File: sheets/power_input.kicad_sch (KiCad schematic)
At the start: 106 parts, among them J2 TYPE-C-31-M-12, Q20 FDMS86250, Q21 FDMC2523P, Q22 BSC057N08NS3 G, Q23 BSC057N08NS3 G, Q24 FCX493TA, Q25 FCX493TA, Q30 IRLR7843TRPBF, Q31 IRLR7843TRPBF, T1 750313355, U10 TPS23730RMTR, U19 LM5050MKX-1/NOPB, U2 CH224K, U20 TCMT1107, U21 LM5050MKX-1/NOPB, U22 TL431IDBVR, U23 FOD817DS

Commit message: sch: audit fixes — buck EN divider corners, 3V3-domain senses, spec §10 LEDs
F1 (critical): TPS565201 BUCK_EN divider (R40/R41) redesigned against the
datasheet's VENH/VENL/REN corners so the 3.3V buck actually starts once the
12V node is negotiated, without false-starting on pre-negotiation 5V VBUS.

F2 (medium): GP18/GP19 retargeted from the RP2040 sheet to the ethernet
sheet's existing 3.3V-domain PERST/CLKREQ shifter outputs; GP17 gets a new
BSS138 level-shift stage (Q40/R122) on m2, mirroring the Task 10 pattern.

F3 (minor): added the two spec §10 indicator LEDs (D29 12V/power, D30
PD-good) that were dropped during Task 4 and never restored.

check_nets.py all pass; ERC 0 errors / 800 warnings (was 788, full delta
accounted in docs/erc-waivers.md); netlist exports clean, no annotation
warnings.

Co-Authored-By: Claude Fable 5 <noreply@anthropic.com>
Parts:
- added D29: Green 0603, LED_0603, symbol Device:LED
- added D30: Blue 0603, LED_0603, symbol Device:LED
- added R120, R121: 1k, R_0603, symbol Device:R_Small
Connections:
- net CH224K_PG: now also D30.1 (K)
- net GND: now also D29.1 (K)
- new net LED_PWR: R120.1, R121.1
- new net N_D29_A: D29.2 (A), R120.2
- new net N_D30_A: D30.2 (A), R121.2
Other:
- note added: "Task 13 audit fix (F3, minor): D29/R120 -- spec S10 12V-node/power indicator, missing since Task 4 dropped the LED (drift, never amended). LED_PWR->R120(1k)->D29->GND. LED_PWR is only alive when +3V3 is up, which -- per the F1 fix pass (R40/R41 BUCK_EN divider corrected) -- only happens once the +12V node has been negotiated (buck now reliably starts ~8V+, never at 5V pre-negotiation). So D29 cor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"
- note added: "Task 13 audit fix (F3, minor): D30/R121 -- spec S10 PD-good indicator, missing since Task 4 dropped the LED. LED_PWR->R121(1k)->D30->CH224K_PG. CH224K_PG is open-drain, active-low (WCH CH224K datasheet: pulls to GND once PD negotiation succeeds; datasheet explicitly lists driving an indicator LED as a typical use). Checked R4 (10k pull-up, CH224K_PG to +3V3, from Task 4): it does NOT conflict wit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"
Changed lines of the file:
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@@
 	)
 	(symbol
+		(lib_id "Device:LED")
+		(at 115 20 0)
+		(unit 1)
+		(exclude_from_sim no)
+		(in_bom yes)
+		(on_board yes)
+		(dnp no)
+		(fields_autoplaced yes)
+		(property "Reference" "D30" (at 117 17 0) (effects (font (size 1.27 1.27))))
+		(property "Value" "Blue 0603" (at 117 23 0) (effects (font (size 1.27 1.27))))
+		(property "Footprint" "LED_0603" (at 115 20 0) (hide yes) (effects (font (size 1.27 1.27))))
+		(property "Datasheet" "" (at 115 20 0) (hide yes) (effects (font (size 1.27 1.27))))
+		(pin "1")
+		(pin "2")
+		(instances
+			(project "sierra-to-usb"
+				(path "/f141b3c0-0a69-4819-acb0-dc32f46a3541/f5a12b4b-c279-4b26-9f14-8d152bf2e4b9"
+					(reference "D30")
+					(unit 1)
+				)
+			)
+		)
+	)
+	(symbol
+		(lib_id "Device:R_Small")
+		(at 115 27 0)
+		(unit 1)
+		(exclude_from_sim no)
+		(in_bom yes)
+		(on_board yes)
+		(dnp no)
+		(fields_autoplaced yes)
+		(property "Reference" "R121" (at 117 24 0) (effects (font (size 1.27 1.27))))
+		(property "Value" "1k" (at 117 30 0) (effects (font (size 1.27 1.27))))
+		(property "Footprint" "R_0603" (at 115 27 0) (hide yes) (effects (font (size 1.27 1.27))))
+		(property "Datasheet" "" (at 115 27 0) (hide yes) (effects (font (size 1.27 1.27))))
+		(pin "1")
+		(pin "2")
+		(instances
+			(project "sierra-to-usb"
+				(path "/f141b3c0-0a69-4819-acb0-dc32f46a3541/f5a12b4b-c279-4b26-9f14-8d152bf2e4b9"
+					(reference "R121")
+					(unit 1)
+				)
+			)
+		)
+	)
+	(symbol
 		(lib_id "sierra-to-usb:MB10S")
 		(at 150 30 0)
@@
 	)
 	(symbol
+		(lib_id "Device:LED")
+		(at 565 143 0)
+		(unit 1)
+		(exclude_from_sim no)
+		(in_bom yes)
+		(on_board yes)
+		(dnp no)
+		(fields_autoplaced yes)
+		(property "Reference" "D29" (at 567 140 0) (effects (font (size 1.27 1.27))))
+		(property "Value" "Green 0603" (at 567 146 0) (effects (font (size 1.27 1.27))))
+		(property "Footprint" "LED_0603" (at 565 143 0) (hide yes) (effects (font (size 1.27 1.27))))
+		(property "Datasheet" "" (at 565 143 0) (hide yes) (effects (font (size 1.27 1.27))))
+		(pin "1")
+		(pin "2")
+		(instances
+			(project "sierra-to-usb"
+				(path "/f141b3c0-0a69-4819-acb0-dc32f46a3541/f5a12b4b-c279-4b26-9f14-8d152bf2e4b9"
+					(reference "D29")
+					(unit 1)
+				)
+			)
+		)
+	)
+	(symbol
+		(lib_id "Device:R_Small")
+		(at 565 150 0)
+		(unit 1)
+		(exclude_from_sim no)
+		(in_bom yes)
+		(on_board yes)
+		(dnp no)
+		(fields_autoplaced yes)
+		(property "Reference" "R120" (at 567 147 0) (effects (font (size 1.27 1.27))))
+		(property "Value" "1k" (at 567 153 0) (effects (font (size 1.27 1.27))))
+		(property "Footprint" "R_0603" (at 565 150 0) (hide yes) (effects (font (size 1.27 1.27))))
+		(property "Datasheet" "" (at 565 150 0) (hide yes) (effects (font (size 1.27 1.27))))
+		(pin "1")
+		(pin "2")
+		(instances
+			(project "sierra-to-usb"
+				(path "/f141b3c0-0a69-4819-acb0-dc32f46a3541/f5a12b4b-c279-4b26-9f14-8d152bf2e4b9"
+					(reference "R120")
+					(unit 1)
+				)
+			)
+		)
+	)
+	(symbol
+		(lib_id "power:GND")
+		(at 561.19 143 0)
+		(unit 1)
+		(exclude_from_sim no)
+		(in_bom yes)
+		(on_board yes)
+		(dnp no)
+		(fields_autoplaced yes)
+		(property "Reference" "#PWR9500001" (at 561.19 141.0 0) (hide yes) (effects (font (size 1.27 1.27))))
+		(property "Value" "GND" (at 561.19 139.0 0) (effects (font (size 1.27 1.27))))
+		(property "Footprint" "" (at 561.19 143 0) (hide yes) (effects (font (size 1.27 1.27))))
+		(property "Datasheet" "" (at 561.19 143 0) (hide yes) (effects (font (size 1.27 1.27))))
+		(pin "1")
+		(instances
+			(project "sierra-to-usb"
+				(path "/f141b3c0-0a69-4819-acb0-dc32f46a3541/f5a12b4b-c279-4b26-9f14-8d152bf2e4b9"
+					(reference "#PWR9500001")
+					(unit 1)
+				)
+			)
+		)
+	)
+	(symbol
 		(lib_id "sierra-to-usb:LM5050-1")
 		(at 580 30 0)
@@
 		(effects (font (size 1.27 1.27)) (justify left bottom))
 	)
+	(global_label "LED_PWR"
+		(shape input)
+		(at 565.0 147.46 0)
+		(effects (font (size 1.016 1.016)) (justify left bottom))
+		(property "Intersheetrefs" "${INTERSHEET_REFS}" (at 565.0 147.46 0) (effects (font (size 1.27 1.27))))
+	)
+	(label "N_D29_A"
+		(at 565.0 152.54 0)
+		(effects (font (size 1.016 1.016)) (justify left bottom))
+	)
+	(label "N_D29_A"
+		(at 568.81 143.0 0)
+		(effects (font (size 1.016 1.016)) (justify left bottom))
+	)
+	(global_label "LED_PWR"
+		(shape input)
+		(at 115.0 24.46 0)
+		(effects (font (size 1.016 1.016)) (justify left bottom))
+		(property "Intersheetrefs" "${INTERSHEET_REFS}" (at 115.0 24.46 0) (effects (font (size 1.27 1.27))))
+	)
+	(label "N_D30_A"
+		(at 115.0 29.54 0)
+		(effects (font (size 1.016 1.016)) (justify left bottom))
+	)
+	(label "N_D30_A"
+		(at 118.81 20.0 0)
+		(effects (font (size 1.016 1.016)) (justify left bottom))
+	)
+	(global_label "CH224K_PG"
+		(shape input)
+		(at 111.19 20.0 0)
+		(effects (font (size 1.016 1.016)) (justify left bottom))
+		(property "Intersheetrefs" "${INTERSHEET_REFS}" (at 111.19 20.0 0) (effects (font (size 1.27 1.27))))
+	)
+	(text "Task 13 audit fix (F3, minor): D29/R120 -- spec S10 12V-node/power indicator, missing since Task 4 dropped the LED (drift, never amended). LED_PWR->R120(1k)->D29->GND. LED_PWR is only alive when +3V3 is up, which -- per the F1 fix pass (R40/R41 BUCK_EN divider corrected) -- only happens once the +12V node has been negotiated (buck now reliably starts ~8V+, never at 5V pre-negotiation). So D29 correctly indicates negotiated-12V-present, not raw VBUS. It is killable via the LED_PWR switch/GPIO like the other LED_PWR-domain indicators (RGB, WWAN)."
+		(exclude_from_sim no)
+		(at 555 160 0)
+		(effects (font (size 1.27 1.27)) (justify left bottom))
+	)
+	(text "Task 13 audit fix (F3, minor): D30/R121 -- spec S10 PD-good indicator, missing since Task 4 dropped the LED. LED_PWR->R121(1k)->D30->CH224K_PG. CH224K_PG is open-drain, active-low (WCH CH224K datasheet: pulls to GND once PD negotiation succeeds; datasheet explicitly lists driving an indicator LED as a typical use). Checked R4 (10k pull-up, CH224K_PG to +3V3, from Task 4): it does NOT conflict with D30 -- it defines a clean idle-high (LED off) state when PG is unasserted and adds only ~0.33mA of extra sink current when PG pulls low (LED on); R4 is kept as-is, not replaced."
+		(exclude_from_sim no)
+		(at 105 5 0)
+		(effects (font (size 1.27 1.27)) (justify left bottom))
+	)

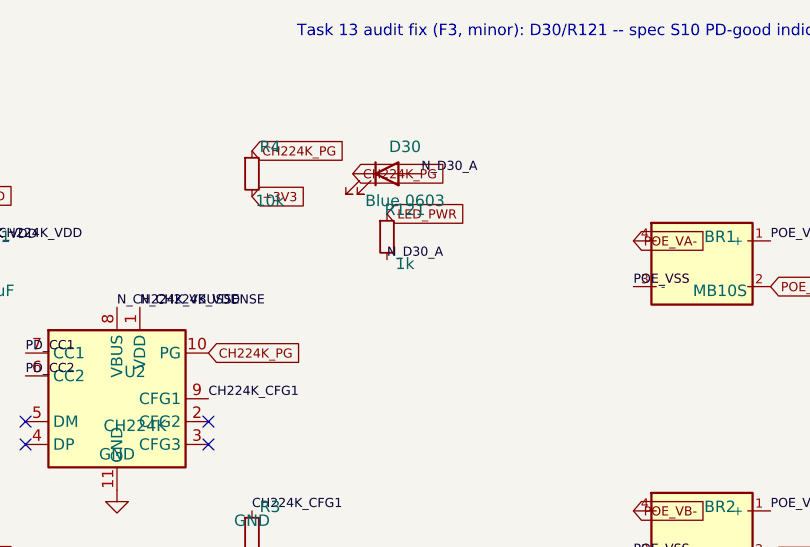
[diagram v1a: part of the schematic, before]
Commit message: sch: footprints + assembly-split BOM fields
Task 14: bind real footprints to all 363 BOM symbols, add Assembly/LCSC/MPN/
Distributor properties to every symbol, and close the accumulated
footprint_link_issues ERC deferral (148 -> 0).

- New fp-lib-table + lib/sierra-to-usb.pretty/ (15 custom footprints
  authored from real manufacturer drawings: magjack, MHF4, SMA edge,
  nano-SIM, MFF2 eSIM, M.2 socket, bridge rectifier, 2x PoE flyback
  inductors, TPS23730 VQFN-45, FDMC2523P, FOD817 gull-wing DIP-4, SK6805
  LED, PoE transformer, and a corrected full-24-pin USB-C receptacle for
  J1 -- the previously-bound stock footprint only exposed 6 of 24 pins).
- Fixed ~120 bare/stale/wrong-library-prefix Footprint strings project-wide.
- Assembly split: 12 JLC rows (all LCSC-backed), 351 HAND rows (MPN +
  Distributor on every one). Disclosed flip: U30 (eSIM) JLC->HAND per
  sourcing.md's own no-LCSC-listing flag, overriding the task's shorthand.
- Carry-forwards closed: D30 series R 1k->560R, INA226 MSOP-10->VSSOP-10
  (+EP-VIA), R39/R44 Kelvin-route note, JP1-3 solder-jumper footprints,
  SW2 silk note, 42x 0402->0603 hand-solder upgrades.
- New tools/check_footprints.py gate: Footprint/Assembly presence, JLC=>LCSC,
  and footprint-pad-count >= symbol-pin-count (parsed from real .kicad_mod
  files + netlist pin lists).
- Recovered sheets/mcu.kicad_sch from a pre-existing uncommitted data-loss
  state (44 symbols missing vs the Task 13 gate-approved commit) before
  applying any Task 14 edits.

Verification: check_footprints.py all-pass, check_nets.py all-pass
(connectivity untouched), kicad-cli sch erc 0 errors.

Two pre-existing issues disclosed but not fixed here (out of footprint-
assignment scope, documented in docs/verification.md and
docs/erc-waivers.md): J1's now-corrected footprint was masking a Task-7
error, and 7 refs (Q20,Q22-25,Q30,Q31) use letter-pinned generic FET/BJT
symbols that will show unmatched pins at PCB import regardless of
footprint choice -- flagge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
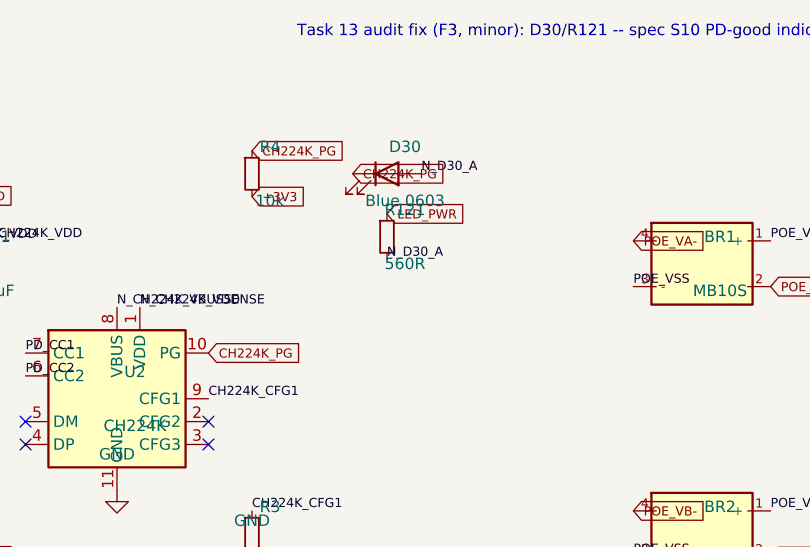
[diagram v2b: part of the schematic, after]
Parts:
- BR1, BR2: footprint Diode_SMD:D_MBS-4 -> sierra-to-usb:D_MBS-4; Assembly (none) -> HAND; Distributor (none) -> LCSC; LCSC (none) -> C2488; MPN (none) -> MB10S
- C1: footprint C_0603 -> Capacitor_SMD:C_0603_1608Metric; Assembly (none) -> HAND; Distributor (none) -> LCSC; MPN (none) -> Generic MLCC 1uF 0603 (Yageo/Murata/Samsung equiv, exact P/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
- C10: footprint C_0805 -> Capacitor_SMD:C_0805_2012Metric; Assembly (none) -> HAND; Distributor (none) -> LCSC; MPN (none) -> Generic MLCC 470pF/100V 0805 (Yageo/Murata/Samsung equiv, e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
- C11: footprint C_0603 -> Capacitor_SMD:C_0603_1608Metric; Assembly (none) -> HAND; Distributor (none) -> LCSC; MPN (none) -> Generic MLCC 2.2nF/50V 0603 (Yageo/Murata/Samsung equiv, ex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
- C12: footprint C_0603 -> Capacitor_SMD:C_0603_1608Metric; Assembly (none) -> HAND; Distributor (none) -> LCSC; MPN (none) -> Generic MLCC 47nF/50V 0603 (Yageo/Murata/Samsung equiv, exa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
- C13, C14: footprint C_0603 -> Capacitor_SMD:C_0603_1608Metric; Assembly (none) -> HAND; Distributor (none) -> LCSC; MPN (none) -> Generic MLCC 0.1uF/25V 0603 (Yageo/Murata/Samsung equiv, ex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
- C15: footprint C_0805 -> Capacitor_SMD:C_0805_2012Metric; Assembly (none) -> HAND; Distributor (none) -> LCSC; MPN (none) -> Generic MLCC 0.1uF/50V 0805 (Yageo/Murata/Samsung equiv, ex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
- C16: footprint C_0805 -> Capacitor_SMD:C_0805_2012Metric; Assembly (none) -> HAND; Distributor (none) -> LCSC; MPN (none) -> Generic MLCC 1uF/25V 0805 (Yageo/Murata/Samsung equiv, exac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
- C17: footprint C_1206 -> Capacitor_SMD:C_1206_3216Metric; Assembly (none) -> HAND; Distributor (none) -> LCSC; MPN (none) -> Generic MLCC 0.047uF/250V 1206 (Yageo/Murata/Samsung equiv,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
- C18: footprint C_0805 -> Capacitor_SMD:C_0805_2012Metric; Assembly (none) -> HAND; Distributor (none) -> LCSC; MPN (none) -> Generic MLCC 0.22uF/50V 0805 (Yageo/Murata/Samsung equiv, e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
- C19: footprint C_1808 -> Capacitor_SMD:C_1808_4520Metric; Assembly (none) -> HAND; Distributor (none) -> LCSC; MPN (none) -> Generic MLCC 2200pF/2kV 1808 (Yageo/Murata/Samsung equiv, e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
- C2: footprint C_0603 -> Capacitor_SMD:C_0603_1608Metric; Assembly (none) -> HAND; Distributor (none) -> LCSC; MPN (none) -> Generic MLCC 1nF 0603 (Yageo/Murata/Samsung equiv, exact P/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
- C20: footprint C_0603 -> Capacitor_SMD:C_0603_1608Metric; Assembly (none) -> HAND; Distributor (none) -> LCSC; MPN (none) -> Generic MLCC 1nF/100V 0603 (Yageo/Murata/Samsung equiv, exa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
- C21, C23: footprint C_1206 -> Capacitor_SMD:C_1206_3216Metric; Assembly (none) -> HAND; Distributor (none) -> LCSC; MPN (none) -> Generic MLCC 0.047uF/100V 1206 (Yageo/Murata/Samsung equiv,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
- C22, C31: footprint C_0603 -> Capacitor_SMD:C_0603_1608Metric; Assembly (none) -> HAND; Distributor (none) -> LCSC; MPN (none) -> Generic MLCC 100pF/25V 0603 (Yageo/Murata/Samsung equiv, ex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
- C24: footprint C_1206 -> Capacitor_SMD:C_1206_3216Metric; Assembly (none) -> HAND; Distributor (none) -> LCSC; MPN (none) -> Generic MLCC 1000pF/100V 1206 (Yageo/Murata/Samsung equiv, 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
- C25: footprint CP_Elec_6.3x5.8 -> Capacitor_SMD:CP_Elec_6.3x5.8; Assembly (none) -> HAND; Distributor (none) -> LCSC; MPN (none) -> Generic MLCC 39uF/16V 0603 (Yageo/Murata/Samsung equiv, exa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
- C26, C27: footprint C_1210 -> Capacitor_SMD:C_1210_3225Metric; Assembly (none) -> HAND; Distributor (none) -> LCSC; MPN (none) -> Generic MLCC 22uF/35V 1210 (Yageo/Murata/Samsung equiv, exa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
- C28: footprint CP_Elec_10x10.5 -> Capacitor_SMD:CP_Elec_10x10.5; Assembly (none) -> HAND; Distributor (none) -> LCSC; MPN (none) -> Generic MLCC 560uF/25V 0603 (Yageo/Murata/Samsung equiv, ex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
- C29: footprint C_0603 -> Capacitor_SMD:C_0603_1608Metric; Assembly (none) -> HAND; Distributor (none) -> LCSC; MPN (none) -> Generic MLCC 68nF/16V 0603 (Yageo/Murata/Samsung equiv, exa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
- C3, C9: footprint C_1206 -> Capacitor_SMD:C_1206_3216Metric; Assembly (none) -> HAND; Distributor (none) -> LCSC; MPN (none) -> Generic MLCC 0.1uF/100V 1206 (Yageo/Murata/Samsung equiv, e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
- C30: footprint C_0805 -> Capacitor_SMD:C_0805_2012Metric; Assembly (none) -> HAND; Distributor (none) -> LCSC; MPN (none) -> Generic MLCC 1uF/50V 0805 (Yageo/Murata/Samsung equiv, exac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
- C32: footprint C_0603 -> Capacitor_SMD:C_0603_1608Metric; Assembly (none) -> HAND; Distributor (none) -> LCSC; MPN (none) -> Generic MLCC 3.9nF/50V 0603 (Yageo/Murata/Samsung equiv, ex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
- C4: footprint CP_Elec_10x13 -> Capacitor_SMD:CP_Elec_10x12.6; Assembly (none) -> HAND; Distributor (none) -> LCSC; MPN (none) -> Generic MLCC 68uF/100V 0603 (Yageo/Murata/Samsung equiv, ex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
- C5, C6, C7: footprint C_1210 -> Capacitor_SMD:C_1210_3225Metric; Assembly (none) -> HAND; Distributor (none) -> LCSC; MPN (none) -> Generic MLCC 2.2uF/100V 1210 (Yageo/Murata/Samsung equiv, e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
- C8: footprint C_0805 -> Capacitor_SMD:C_0805_2012Metric; Assembly (none) -> HAND; Distributor (none) -> LCSC; MPN (none) -> Generic MLCC 0.1uF/100V 0805 (Yageo/Murata/Samsung equiv, e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
- D1, D2, D3, D4, D5, D8: footprint D_SOD-123 -> Diode_SMD:D_SOD-123; Assembly (none) -> HAND; Distributor (none) -> LCSC; MPN (none) -> ON Semi MMSD914T1G
- D12, D13: footprint D_SMA -> Diode_SMD:D_SMA; Assembly (none) -> HAND; Distributor (none) -> LCSC; MPN (none) -> ON Semi MURA110T3G
- D14, D9: footprint D_SOD-123 -> Diode_SMD:D_SOD-123; Assembly (none) -> HAND; Distributor (none) -> LCSC; MPN (none) -> MMSZ5242B-7-F
- D15: Assembly (none) -> HAND; Distributor (none) -> LCSC; MPN (none) -> ON Semi BAT54S-7-F
- D16: footprint LED_0603 -> LED_SMD:LED_0603_1608Metric; Assembly (none) -> HAND; Distributor (none) -> LCSC; MPN (none) -> Generic yellow 0603 LED (Yageo/Everlight equiv)
- D29: footprint LED_0603 -> LED_SMD:LED_0603_1608Metric; Assembly (none) -> HAND; Distributor (none) -> LCSC; MPN (none) -> Generic green 0603 LED (Yageo/Everlight equiv)
- D30: footprint LED_0603 -> LED_SMD:LED_0603_1608Metric; Assembly (none) -> HAND; Distributor (none) -> LCSC; MPN (none) -> Generic blue 0603 LED (Yageo/Everlight equiv)
- D6: footprint Diode_SMB:D_SMB -> Diode_SMD:D_SMB; Assembly (none) -> HAND; Distributor (none) -> LCSC; LCSC (none) -> C19077533; MPN (none) -> SMAJ13A
- D7: footprint Diode_SMB:D_SMB -> Diode_SMD:D_SMB; Assembly (none) -> HAND; Distributor (none) -> LCSC; LCSC (none) -> C19077554; MPN (none) -> SMAJ58A
- J2: footprint (none) -> Connector_USB:USB_C_Receptacle_HRO_TYPE-C-31-M-12; Assembly (none) -> HAND; Distributor (none) -> LCSC; LCSC (none) -> C165948; MPN (none) -> HRO TYPE-C-31-M-12
- L1: footprint L_18x18 -> sierra-to-usb:L_Wurth_WE-HCI_74435571500; Assembly (none) -> HAND; Distributor (none) -> DigiKey; MPN (none) -> Wurth 74435571500
- L2: footprint L_WE-HC6 -> sierra-to-usb:L_Wurth_WE-HCI_744325550; Assembly (none) -> HAND; Distributor (none) -> DigiKey; MPN (none) -> Wurth 744325550
- L3: footprint L_7x7 -> Inductor_SMD:L_6.3x6.3_H3; Assembly (none) -> HAND; Distributor (none) -> LCSC; LCSC (none) -> C2042369; MPN (none) -> Bourns SRR6603-222ML
- Q20: footprint Package_DFN_QFN:PQFN08A -> Package_DFN_QFN:PQFN-8-EP_6x5mm_P1.27mm_Generic; Assembly (none) -> HAND; Distributor (none) -> DigiKey; EP-VIA (none) -> yes; MPN (none) -> ON Semi FDMS86250
- Q21: footprint Package_DFN_QFN:QFN-8_2x2mm -> sierra-to-usb:FDMC2523P; Assembly (none) -> HAND; Distributor (none) -> DigiKey; MPN (none) -> ON Semi FDMC2523P
- Q22, Q23: footprint Package_TO_SOT_SMD:PG-TDSON-8 -> Package_TO_SOT_SMD:TDSON-8-1; Assembly (none) -> HAND; Distributor (none) -> DigiKey; EP-VIA (none) -> yes; MPN (none) -> Infineon BSC057N08NS3G
- Q24, Q25: Assembly (none) -> HAND; Distributor (none) -> LCSC; MPN (none) -> Central Semi FCX493TA
- Q30, Q31: Assembly (none) -> HAND; Distributor (none) -> DigiKey; MPN (none) -> Infineon IRLR7843TRPBF
- R1, R120, R34, R36: footprint R_0603 -> Resistor_SMD:R_0603_1608Metric; Assembly (none) -> HAND; Distributor (none) -> LCSC; MPN (none) -> Yageo RC0603JR-071KL
- R10: footprint R_0603 -> Resistor_SMD:R_0603_1608Metric; Assembly (none) -> HAND; Distributor (none) -> LCSC; MPN (none) -> Yageo RC0603JR-07110KL
- R11, R18, R2, R33, R37, R38, R4: footprint R_0603 -> Resistor_SMD:R_0603_1608Metric; Assembly (none) -> HAND; Distributor (none) -> LCSC; MPN (none) -> Yageo RC0603JR-0710KL
- R12: footprint R_0603 -> Resistor_SMD:R_0603_1608Metric; Assembly (none) -> HAND; Distributor (none) -> LCSC; MPN (none) -> Yageo RC0603JR-07237KL
- R121: value 1k -> 560R; footprint R_0603 -> Resistor_SMD:R_0603_1608Metric; Assembly (none) -> HAND; Distributor (none) -> LCSC; MPN (none) -> Yageo RC0603JR-071KL
- R13: footprint R_0603 -> Resistor_SMD:R_0603_1608Metric; Assembly (none) -> HAND; Distributor (none) -> LCSC; MPN (none) -> Yageo RC0603JR-0760K4L
- R14: footprint R_0603 -> Resistor_SMD:R_0603_1608Metric; Assembly (none) -> HAND; Distributor (none) -> LCSC; MPN (none) -> Yageo RC0603JR-0749K9L
- R15: footprint R_0603 -> Resistor_SMD:R_0603_1608Metric; Assembly (none) -> HAND; Distributor (none) -> LCSC; MPN (none) -> Yageo RC0603JR-0742K2L
- R16: footprint R_0603 -> Resistor_SMD:R_0603_1608Metric; Assembly (none) -> HAND; Distributor (none) -> LCSC; MPN (none) -> Yageo RC0603JR-07499KL
- R17: footprint R_0603 -> Resistor_SMD:R_0603_1608Metric; Assembly (none) -> HAND; Distributor (none) -> LCSC; MPN (none) -> Yageo RC0603JR-0710RL
- R19: footprint R_0603 -> Resistor_SMD:R_0603_1608Metric; Assembly (none) -> HAND; Distributor (none) -> LCSC; MPN (none) -> Yageo RC0603JR-073KL
- R20: footprint R_1206 -> Resistor_SMD:R_1206_3216Metric; Assembly (none) -> HAND; Distributor (none) -> LCSC; MPN (none) -> Generic 0.05/1W 1206 resistor (order-time equiv)
- R21: footprint R_1206 -> Resistor_SMD:R_1206_3216Metric; Assembly (none) -> HAND; Distributor (none) -> LCSC; MPN (none) -> Yageo RC1206JR-074K02L
- R22: footprint R_1206 -> Resistor_SMD:R_1206_3216Metric; Assembly (none) -> HAND; Distributor (none) -> LCSC; MPN (none) -> Yageo RC1206JR-078K06L
- R23, R31, R32, R35: footprint R_0603 -> Resistor_SMD:R_0603_1608Metric; Assembly (none) -> HAND; Distributor (none) -> LCSC; MPN (none) -> Yageo RC0603JR-072KL
- R24: footprint R_0805 -> Resistor_SMD:R_0805_2012Metric; Assembly (none) -> HAND; Distributor (none) -> LCSC; MPN (none) -> Yageo RC0805JR-075R1L
- R25, R26: footprint R_2512 -> Resistor_SMD:R_2512_6332Metric; Assembly (none) -> HAND; Distributor (none) -> LCSC; MPN (none) -> Generic 10k/1W 2512 resistor (order-time equiv)
- R27: footprint R_2512 -> Resistor_SMD:R_2512_6332Metric; Assembly (none) -> HAND; Distributor (none) -> LCSC; MPN (none) -> Generic 100/1W 2512 resistor (order-time equiv)
- R28: footprint R_0603 -> Resistor_SMD:R_0603_1608Metric; Assembly (none) -> HAND; Distributor (none) -> LCSC; MPN (none) -> Yageo RC0603JR-0749R9L
- R29: footprint R_0603 -> Resistor_SMD:R_0603_1608Metric; Assembly (none) -> HAND; Distributor (none) -> LCSC; MPN (none) -> Yageo RC0603JR-0740K2L
- R3: footprint R_0603 -> Resistor_SMD:R_0603_1608Metric; Assembly (none) -> HAND; Distributor (none) -> LCSC; MPN (none) -> Yageo RC0603JR-0724KL
- R30: footprint R_0603 -> Resistor_SMD:R_0603_1608Metric; Assembly (none) -> HAND; Distributor (none) -> LCSC; MPN (none) -> Yageo RC0603JR-0710K5L
- R5: footprint R_0603 -> Resistor_SMD:R_0603_1608Metric; Assembly (none) -> HAND; Distributor (none) -> LCSC; MPN (none) -> Yageo RC0603JR-071ML
- R6: footprint R_0603 -> Resistor_SMD:R_0603_1608Metric; Assembly (none) -> HAND; Distributor (none) -> LCSC; MPN (none) -> Yageo RC0603JR-0725K5L
- R7, R8: footprint R_0805 -> Resistor_SMD:R_0805_2012Metric; Assembly (none) -> HAND; Distributor (none) -> LCSC; MPN (none) -> Yageo RC0805JR-0732RL
- R9: footprint R_0603 -> Resistor_SMD:R_0603_1608Metric; Assembly (none) -> HAND; Distributor (none) -> LCSC; MPN (none) -> Yageo RC0603JR-0715KL
- T1: footprint Transformer_SMT_XFRMR_29MM08_23MM1 -> sierra-to-usb:Transformer_SMT_WE750313355; Assembly (none) -> HAND; Distributor (none) -> DigiKey; MPN (none) -> Wurth 750313355
- U10: footprint Package_DFN_QFN:QFN-45-1EP_7x5mm_P0.4mm_EP3.6x3.4mm -> sierra-to-usb:TPS23730_RMTR; Assembly (none) -> HAND; Distributor (none) -> DigiKey; EP-VIA (none) -> yes; MPN (none) -> TI TPS23730RMTR
- U19, U21: Assembly (none) -> HAND; Distributor (none) -> DigiKey; MPN (none) -> TI LM5050MKX-1/NOPB
- U2: Assembly (none) -> HAND; Distributor (none) -> LCSC; EP-VIA (none) -> yes; LCSC (none) -> C970725; MPN (none) -> WCH CH224K
- U20: Assembly (none) -> HAND; Distributor (none) -> LCSC; MPN (none) -> Vishay TCMT1107
- U22: Assembly (none) -> HAND; Distributor (none) -> LCSC; MPN (none) -> TI TL431IDBVR
- U23: footprint Package_DIP:DIP-4_W7.62mm_SMDGullWing -> sierra-to-usb:DIP-4_SMD_GullWing_FOD817; Assembly (none) -> HAND; Distributor (none) -> LCSC; MPN (none) -> Onsemi FOD817DS
